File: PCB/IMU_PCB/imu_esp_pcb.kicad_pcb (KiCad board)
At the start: 2 copper layers, 48.5 x 26 mm, 22 parts, among them J3 Conn_01x02_Pin, U1 MPU-6050, U2 ESP32-C3-WROOM-02, U3 PTS647SM38SMTR2LFS, U4 XC6206P332MR-G, U5 1N5819HW-7-F

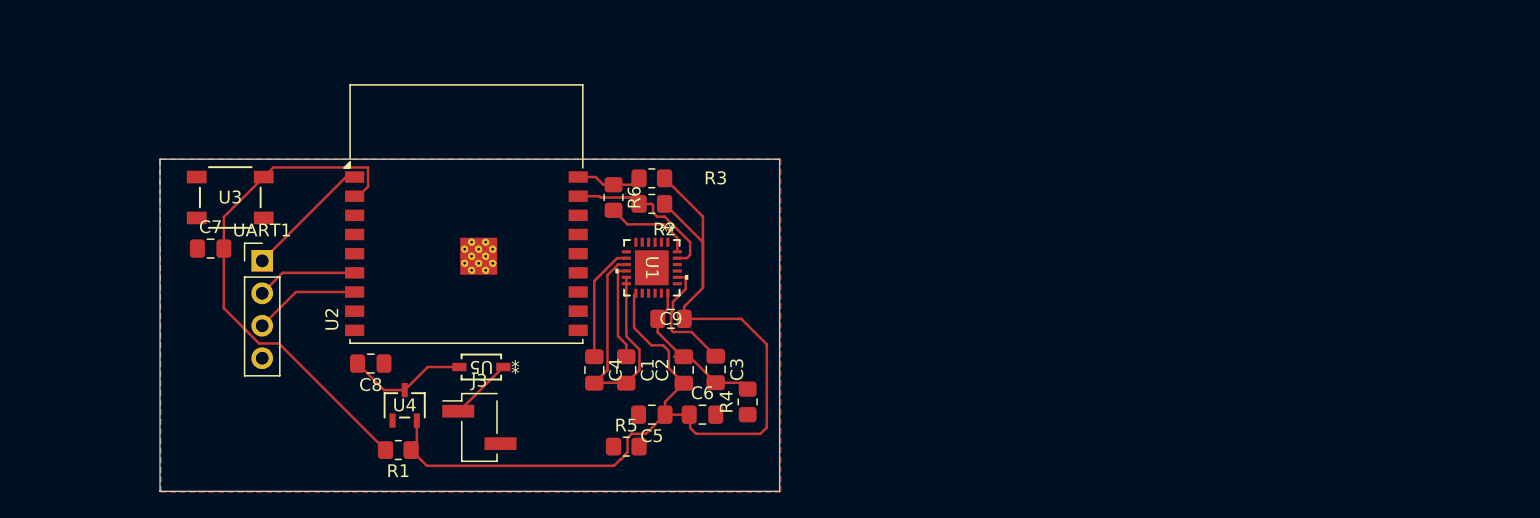
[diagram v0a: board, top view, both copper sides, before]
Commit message: IMU PCB design and schematics updated
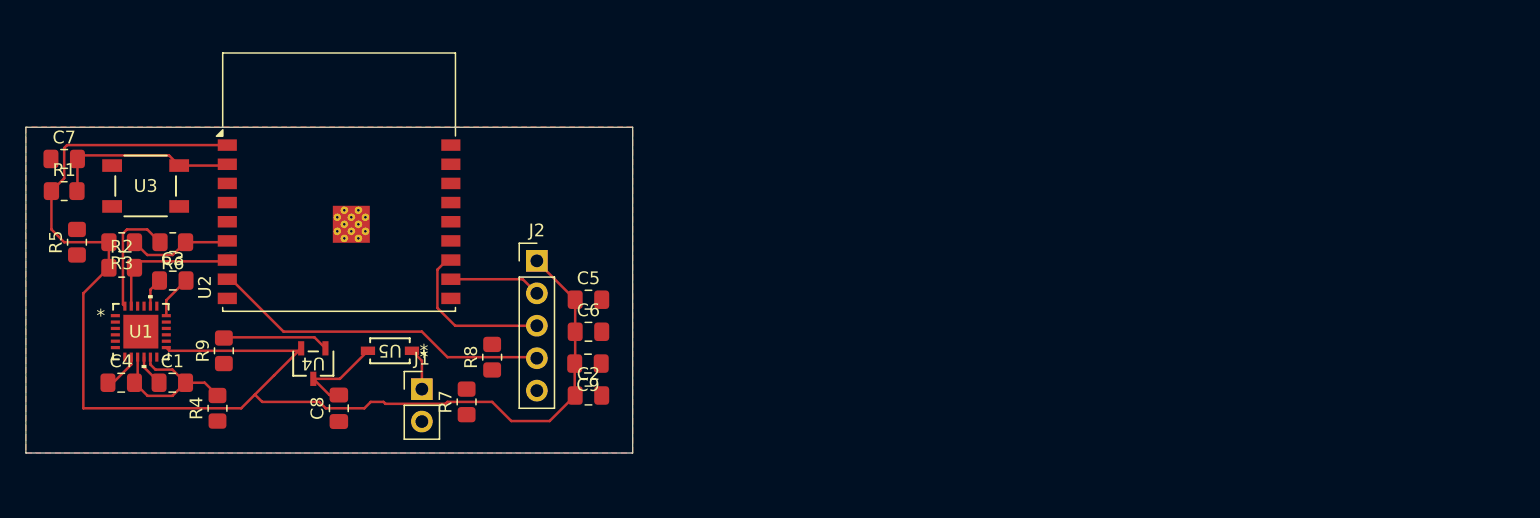
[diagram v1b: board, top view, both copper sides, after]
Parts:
- removed J3: Conn_01x02_Pin, Connector_PinHeader_2.54mm:PinHeader_1x02_P2.54mm_Vertical_SMD_Pin1Left
- removed UART1: UART, Connector_PinHeader_2.54mm:PinHeader_1x04_P2.54mm_Vertical
- added J1: Conn_01x02_Pin, Connector_PinHeader_2.54mm:PinHeader_1x02_P2.54mm_Vertical, F.Cu at (79.0, 86.0)
- added J2: Conn_01x05_Pin, Connector_PinHeader_2.54mm:PinHeader_1x05_P2.54mm_Vertical, F.Cu at (88.0, 76.0)
- added R7: 0, Resistor_SMD:R_0805_2012Metric_Pad1.20x1.40mm_HandSolder, F.Cu at (82.5, 87.0)
- added R8: 0, Resistor_SMD:R_0805_2012Metric_Pad1.20x1.40mm_HandSolder, F.Cu at (84.5, 83.5)
- added R9: 0, Resistor_SMD:R_0805_2012Metric_Pad1.20x1.40mm_HandSolder, F.Cu at (63.5, 83.0)
- moved R5 45.9 mm to (52.0, 74.5), turned to 90 degrees
- moved C3 43.1 mm to (59.5, 77.5), turned to 0 degrees
- moved R2 41.8 mm to (55.5, 76.5), turned to 0 degrees
- moved R3 41.8 mm to (55.5, 74.5), turned to 180 degrees
- moved R4 41.5 mm to (63.0, 87.5)
- moved U1 40.3 mm to (57.0, 81.5), turned to 0 degrees
- moved C4 37.1 mm to (55.5, 85.5), turned to 0 degrees
- moved C1 35.6 mm to (59.5, 85.5), turned to 0 degrees
- moved R6 34.7 mm to (59.5, 74.5), turned to 180 degrees
- moved R1 33.1 mm to (51.0, 70.5), turned to 0 degrees
- moved C7 13.4 mm to (51.0, 68.0)
- moved C6 11.0 mm to (92.0, 81.5)
- moved U2 10.3 mm to (72.5, 72.9)
- moved C5 10.3 mm to (92.0, 79.0), turned to 0 degrees
- moved U4 7.87 mm to (70.5, 84.0), turned to 180 degrees
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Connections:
- U1 pad 12: GND -> unconnected-(U1-INT-Pad12)
- U2 pad 11: unconnected-(U2-IO20/RXD-Pad11) -> RXD
- U2 pad 12: unconnected-(U2-IO21/TXD-Pad12) -> TXD
- U2 pad 17: SCL -> unconnected-(U2-IO1-Pad17)
- U2 pad 18: SDA -> unconnected-(U2-IO0-Pad18)
- U2 pad 6: Net-(U2-IO7) -> SDA
- U2 pad 7: Net-(U2-IO8) -> SCL
- U2 pad 8: unconnected-(U2-IO9-Pad8) -> Net-(J2-Pin_4)
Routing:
- net Net-(J2-Pin_4): track 0.00 -> 26.8 mm
- net RESET: track 40.2 -> 14.8 mm
- net +3.3V: track 91.3 -> 107.2 mm
- net TXD: track 0.00 -> 12.7 mm
- net GND: track 36.1 -> 25.5 mm
- net Net-(U2-IO8): track 8.33 -> 0.00 mm
- net Net-(U2-IO7): track 7.90 -> 0.00 mm
- net Net-(U1-CPOUT): track 9.54 -> 2.30 mm
- net RXD: track 0.00 -> 7.19 mm
- net Net-(U1-VLOGIC): track 9.17 -> 3.00 mm
- net Net-(U1-REGOUT): track 7.60 -> 2.51 mm
- net SDA: track 5.22 -> 8.14 mm
- net Net-(U1-SDA): track 6.98 -> 9.20 mm
- net SCL: track 12.7 -> 10.6 mm
- net Net-(U4-VIN): track 9.58 -> 7.71 mm
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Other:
- board size 48.5 x 26 mm -> 47.5 x 25.5 mm

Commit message: PCB for IMU
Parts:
- removed C1, C2: 0.1 uf, Capacitor_SMD:C_0805_2012Metric_Pad1.18x1.45mm_HandSolder
- removed C3: 2.2 nf, Capacitor_SMD:C_0805_2012Metric_Pad1.18x1.45mm_HandSolder
- removed C4: 10 nf, Capacitor_SMD:C_0805_2012Metric_Pad1.18x1.45mm_HandSolder
- removed R2, R3: 5K, Resistor_SMD:R_0805_2012Metric_Pad1.20x1.40mm_HandSolder
- removed R6, R8, R9: 0, Resistor_SMD:R_0805_2012Metric_Pad1.20x1.40mm_HandSolder
- removed U1: MPU-6050, footprints:QFN24_4X4X0P9-0P5_TDK
- added C10: 100 nf, Capacitor_SMD:C_0805_2012Metric_Pad1.18x1.45mm_HandSolder, F.Cu at (128.0, 81.5)
- added C11: 100 nf, Capacitor_SMD:C_0805_2012Metric_Pad1.18x1.45mm_HandSolder, F.Cu at (128.0, 79.5)
- added R10: 4.7K, Resistor_SMD:R_0805_2012Metric_Pad1.20x1.40mm_HandSolder, F.Cu at (130.0, 71.5)
- added R11: 4.7K, Resistor_SMD:R_0805_2012Metric_Pad1.20x1.40mm_HandSolder, F.Cu at (130.0, 73.5)
- added U6: BMI270, BMI270:BMI270_BOS, F.Cu at (128.8, 76.8)
- moved R5 84.3 mm to (136.0, 82.0)
- moved R1 72.1 mm to (123.0, 67.0)
- moved U3 72.0 mm to (129.4, 67.5)
- moved C7 72.0 mm to (123.0, 69.5)
- moved U2 71.0 mm to (143.5, 70.8)
- moved J2 70.0 mm to (158.0, 78.1), turned to 180 degrees
- moved U5 70.0 mm to (146.5, 81.0)
- moved U4 69.6 mm to (140.0, 81.0), turned to -90 degrees
- moved C8 68.0 mm to (140.5, 85.5)
- moved J1 68.0 mm to (147.0, 85.5), turned to -90 degrees
- moved R4 61.5 mm to (124.0, 79.5), turned to 0 degrees
- moved R7 43.3 mm to (124.0, 74.5), turned to 0 degrees
- moved C5 41.2 mm to (133.0, 83.0), turned to -90 degrees
- moved C6 32.4 mm to (123.0, 72.0), turned to 180 degrees
- moved C9 31.7 mm to (123.0, 77.0), turned to 0 degrees
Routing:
- net +3.3V: track 107.2 -> 85.0 mm
- net GND: track 25.5 -> 15.9 mm
- net Net-(U1-SDA): track 9.20 -> 0.00 mm
- net TXD: track 12.7 -> 6.04 mm
- net Net-(J2-Pin_4): track 26.8 -> 32.0 mm
- net Net-(U1-VLOGIC): track 3.00 -> 0.00 mm
- net SCL: track 10.6 -> 7.93 mm
- net Net-(U1-REGOUT): track 2.51 -> 0.00 mm
- net Net-(U1-CPOUT): track 2.30 -> 0.00 mm
- net SDA: track 8.14 -> 9.85 mm
- net Net-(J1-Pin_1): track 3.32 -> 5.01 mm
- net RXD: track 7.19 -> 5.83 mm
- net RESET: track 14.8 -> 13.9 mm
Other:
- board size 47.5 x 25.5 mm -> 42 x 25 mm

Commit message: IMU PCB updated
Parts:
- removed R4, R5, R7: 0, Resistor_SMD:R_0805_2012Metric_Pad1.20x1.40mm_HandSolder
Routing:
- net Net-(J2-Pin_4): track 32.0 -> 25.4 mm, vias 0 -> 2
- net +3.3V: track 85.0 -> 90.1 mm, vias 0 -> 9
- net GND: track 15.9 -> 12.8 mm
- added copper zone on B.Cu, net GND

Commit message: Finalized Updated IMU PCB
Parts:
- added C1: UCS2G100MPD1TD, AlCap:U1-T_NCH, F.Cu at (154.0, 82.5)
- moved J2 3.96 mm to (161.0, 75.5)
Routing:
- net +3.3V: track 90.1 -> 99.1 mm, vias 9 -> 10
- net TXD: track 6.04 -> 10.1 mm
- net Net-(J2-Pin_4): track 25.4 -> 29.4 mm
- net RXD: track 5.83 -> 9.67 mm
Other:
- board size 42 x 25 mm -> 44.5 x 25 mm
